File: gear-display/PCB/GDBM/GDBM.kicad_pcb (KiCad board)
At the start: 2 copper layers, 96 x 87 mm, 91 parts, among them J1 Con_Screw_1x04_691313510004, J2 Con_Screw_1x04_691313510004, J3 DC_2.5_5.5_PJ-090BH, J4 Con_Screw_1x04_691313510004, J5 Con_Screw_1x04_691313510004, J6 Con_Screw_1x04_691313510004, J7 Con_Screw_1x04_691313510004, J8 USB_B_V_Adam_USB-B-S-VT, M1 Knob_6mm_BL_RED_CLIFF_CL17084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, Q1 PMOS_30V_4A1_SIL3407-TP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

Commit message: fixes
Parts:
- D3: footprint KD_Diode:LED_0603_1608Metric_Pad1.05x0.95mm_HandSolder -> KD_Diode:DIOC1608X70
- turned U1 to -90 degrees
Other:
- board text added: "Changes"
- board text added: "U4, D3, U1, 7-seg display footprints"

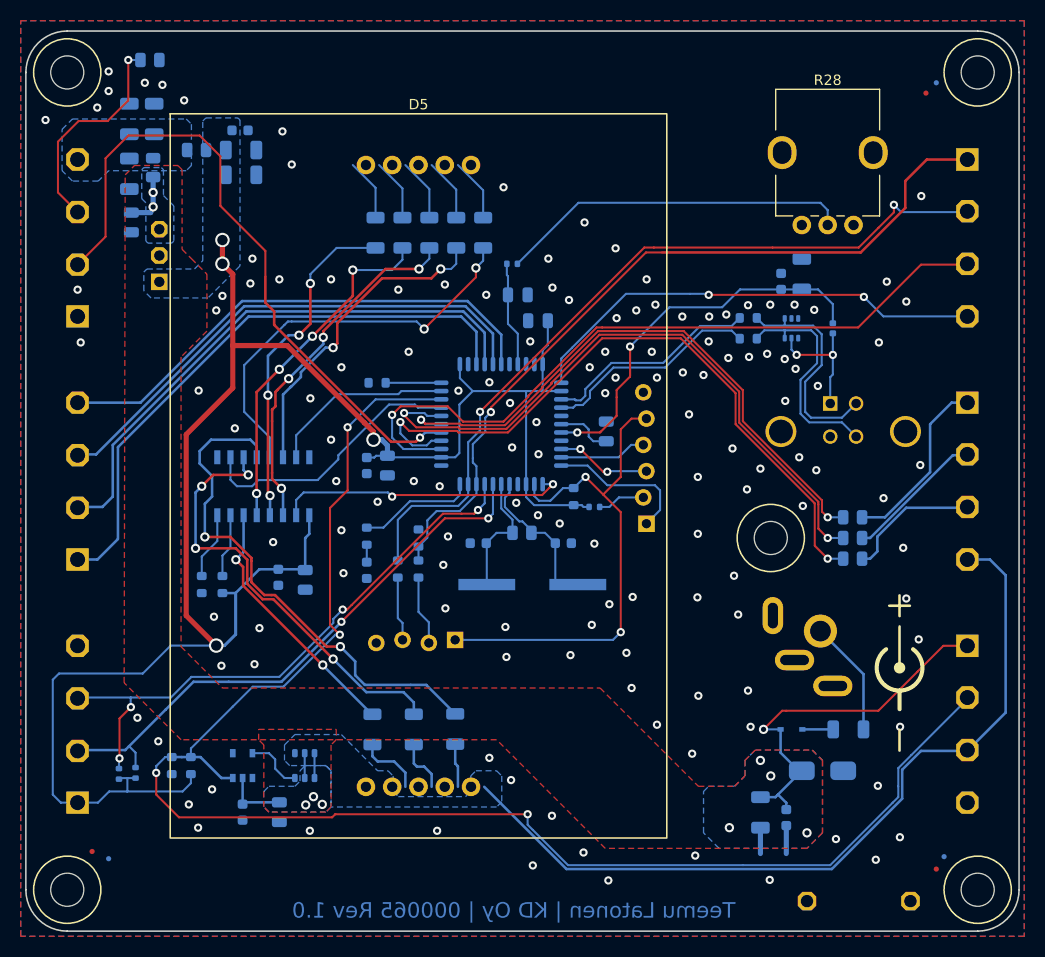
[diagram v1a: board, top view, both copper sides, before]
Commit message: bugfixes
added 555 circuit for brightness control
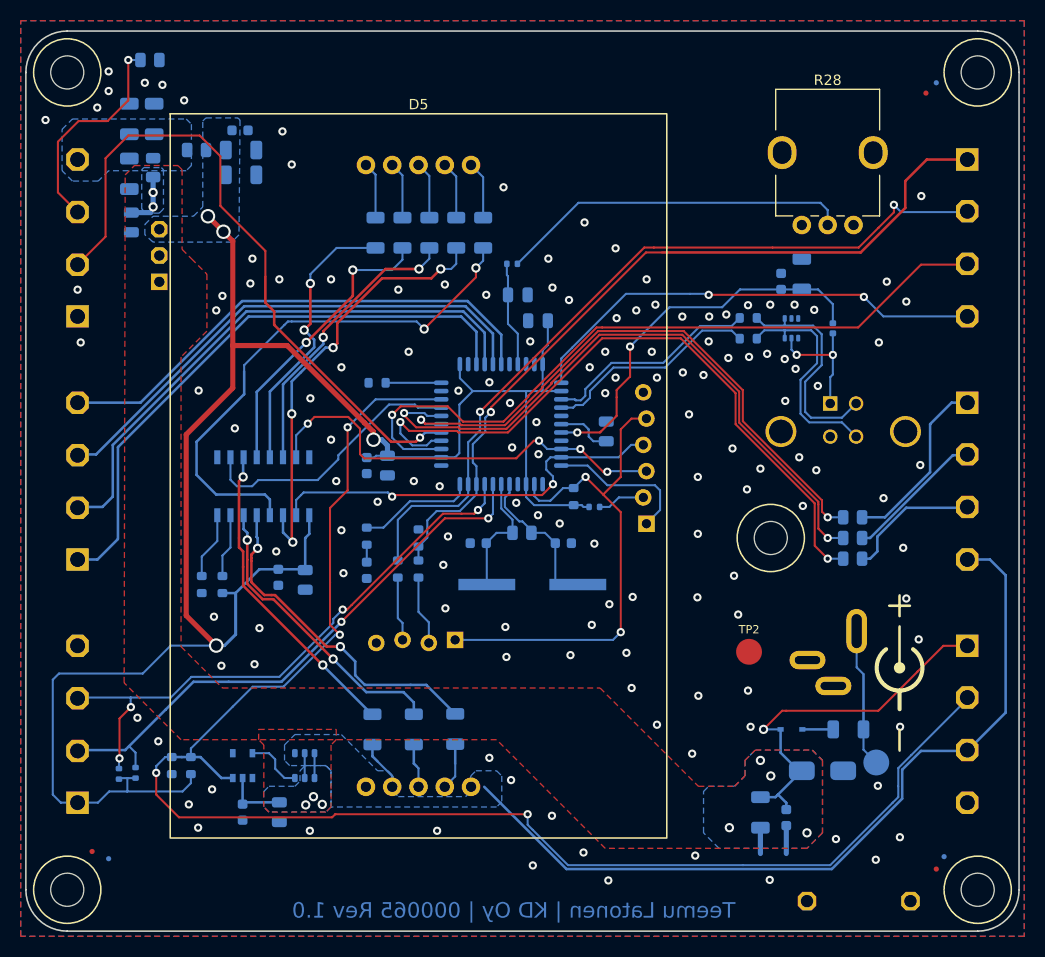
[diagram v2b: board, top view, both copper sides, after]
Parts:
- added TP1: TestPoint_2.5mm_Round, KD_Connector_Pads:TestPoint_Pad_D2.5mm, B.Cu at (165.2, 140.7)
- added TP2: TestPoint_2.5mm_Round, KD_Connector_Pads:TestPoint_Pad_D2.5mm, F.Cu at (152.9, 130.0)
- J3: value DC_2.5_5.5_PJ-090BH -> DC_2.1_5.5_54-00286; footprint KD_Connector_Circular:CON_DC_2.5_5.5_PJ-090BH -> KD_Connector_Circular:CON_DC_2.1_5.5_Tensility_54-00286
- U1: value DC_DC_5V_0A5_K78U05-500R3 -> DC_DC_5V_2A0_GAPTEC_OKI-78SR-5_H
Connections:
- net /MCU/A4(D22) renamed /Brightness Control/PWM_drive
- U2 pad 12: /LED Driver 3/SER_IN -> /MCU/D11
- U2 pad 32: /LED Driver 3/SRCK -> /MCU/D13
- U4 pad 11: /7-Segment Display/d -> /7-Segment Display/e
- U4 pad 12: /7-Segment Display/c -> /7-Segment Display/f
- U4 pad 13: /7-Segment Display/b -> /7-Segment Display/g
- U4 pad 14: /7-Segment Display/a -> /7-Segment Display/dp
- U4 pad 15: /LED Driver 3/SRCK -> /MCU/SCLK
- U4 pad 2: /LED Driver 3/SER_IN -> /MCU/MOSI
- U4 pad 3: /7-Segment Display/dp -> /7-Segment Display/a
- U4 pad 4: /7-Segment Display/g -> /7-Segment Display/b
- U4 pad 5: /7-Segment Display/f -> /7-Segment Display/c
- U4 pad 6: /7-Segment Display/e -> /7-Segment Display/d
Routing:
- net /MCU/SCLK: track 9.17 -> 41.9 mm, vias 2 -> 4
- net /MCU/MOSI: track 8.43 -> 39.7 mm, vias 0 -> 2
- net /LED Driver 3/SER_IN: track 28.2 -> 0.00 mm, vias 2 -> 0
- net /LED Driver 3/SRCK: track 18.0 -> 0.00 mm
- net /7-Segment Display/c: track 49.9 -> 32.5 mm
- net /7-Segment Display/d: track 42.8 -> 28.8 mm, vias 4 -> 2
- net /7-Segment Display/b: track 39.7 -> 51.7 mm
- net /7-Segment Display/a: track 31.1 -> 41.9 mm, vias 2 -> 4
- net /7-Segment Display/dp: track 34.4 -> 28.0 mm, vias 4 -> 2
- net /7-Segment Display/f: track 33.8 -> 28.3 mm, vias 4 -> 2
- net /7-Segment Display/g: track 32.9 -> 27.5 mm, vias 4 -> 2
- net /7-Segment Display/e: track 25.2 -> 30.4 mm
- net +5V: track 181.6 -> 184.5 mm
- net Net-(F1-Pad1): track 11.2 -> 13.5 mm
- net Net-(D5-Pad2): track 6.34 -> 4.88 mm
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
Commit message: layout
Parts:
- added C23: C_0603_10n_X7R_100V, KD_Capacitor:CAPC1608X90N, B.Cu at (141.0, 76.5)
- added C24: C_0603_10n_X7R_100V, KD_Capacitor:CAPC1608X90N, B.Cu at (132.5, 82.5)
- added D6: Schottky_30V_1A_Toshiba_CUS10S30, KD_Diode:D_SOD-323, B.Cu at (148.5, 81.0)
- added D7: Schottky_30V_1A_Toshiba_CUS10S30, KD_Diode:D_SOD-323, B.Cu at (146.0, 81.0)
- added R33: R_0805_1200_5%, KD_Resistor:RESC2012X60N, B.Cu at (147.0, 84.5)
- added U5: Timer_Oscillator_TLC555CDG4, KD_Package_SO:SOIC127P600X175-8, B.Cu at (139.0, 81.0)
- C1, C12, C16, C17, C18, C2, C3: value C_1206_10u_50V -> C_1206_10u_X5R_50V_automotive
- R29: value R_0402_4700_1% -> R_0603_DNP; footprint KD_Resistor:RESC1005X40N -> KD_Resistor:RESC1608X55N_DNP
- moved C21 13.8 mm to (141.6, 87.2)
- moved R29 9.36 mm to (136.1, 85.4), turned to 0 degrees
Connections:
- C21 pad 1: /Brightness Control/POT_W -> +5V
- R28 pad 1: +3V3 -> Net-(D7-Pad1)
- R28 pad 2: Net-(R28-Pad2) -> Net-(C24-Pad2)
- R28 pad 3: Earth -> Net-(D6-Pad2)
- R29 pad 1: Net-(R28-Pad2) -> /Brightness Control/PWM_drive
- R29 pad 2: /Brightness Control/POT_W -> Net-(C24-Pad2)
- U2 pad 31: /7-Segment Display/PWM -> /Brightness Control/PWM_drive
- U2 pad 40: /Brightness Control/PWM_drive -> /MCU/A4(D22)
- U2 pad 41: /Brightness Control/POT_W -> /7-Segment Display/PWM
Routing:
- net Net-(C24-Pad2): track 0.00 -> 51.5 mm
- net /7-Segment Display/PWM: track 152.9 -> 192.3 mm, vias 4 -> 7
- net +5V: track 184.5 -> 220.7 mm, vias 4 -> 6
- net Net-(R28-Pad2): track 34.2 -> 0.00 mm
- net Net-(D7-Pad1): track 0.00 -> 27.9 mm
- net /Brightness Control/PWM_drive: track 0.00 -> 27.5 mm, vias 0 -> 2
- net Net-(D6-Pad2): track 0.00 -> 13.9 mm
- net Net-(D6-Pad1): track 0.00 -> 12.8 mm
- net /Brightness Control/POT_W: track 10.1 -> 0.00 mm
- net Net-(C23-Pad1): track 0.00 -> 2.63 mm
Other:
- board text added: "Teemu Latonen | KD Oy | 000065 Rev 2.0"
- board text removed: "Teemu Latonen | KD Oy | 000065 Rev 1.0"

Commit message: Added a ferrite and silk screen markings
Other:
- board text added: "+"
- board text added: "-"
- board text added: "B"
- board text added: "D"
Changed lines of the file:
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@@
     (effects (font (size 1.5 1.5) (thickness 0.3)) (justify mirror))
+  )
+  (gr_text "+" (at 85.1 82.4) (layer "F.SilkS")
+    (effects (font (size 1.5 1.5) (thickness 0.2)))
+  )
+  (gr_text "D" (at 85.1 92.6) (layer "F.SilkS")
+    (effects (font (size 1.5 1.5) (thickness 0.2)))
+  )
+  (gr_text "-" (at 85.1 97.5) (layer "F.SilkS")
+    (effects (font (size 1.5 1.5) (thickness 0.2)))
+  )
+  (gr_text "B" (at 85.1 87.6) (layer "F.SilkS")
+    (effects (font (size 1.5 1.5) (thickness 0.2)))
   )
   (gr_text "Changes" (at 102 193.5) (layer "Cmts.User")

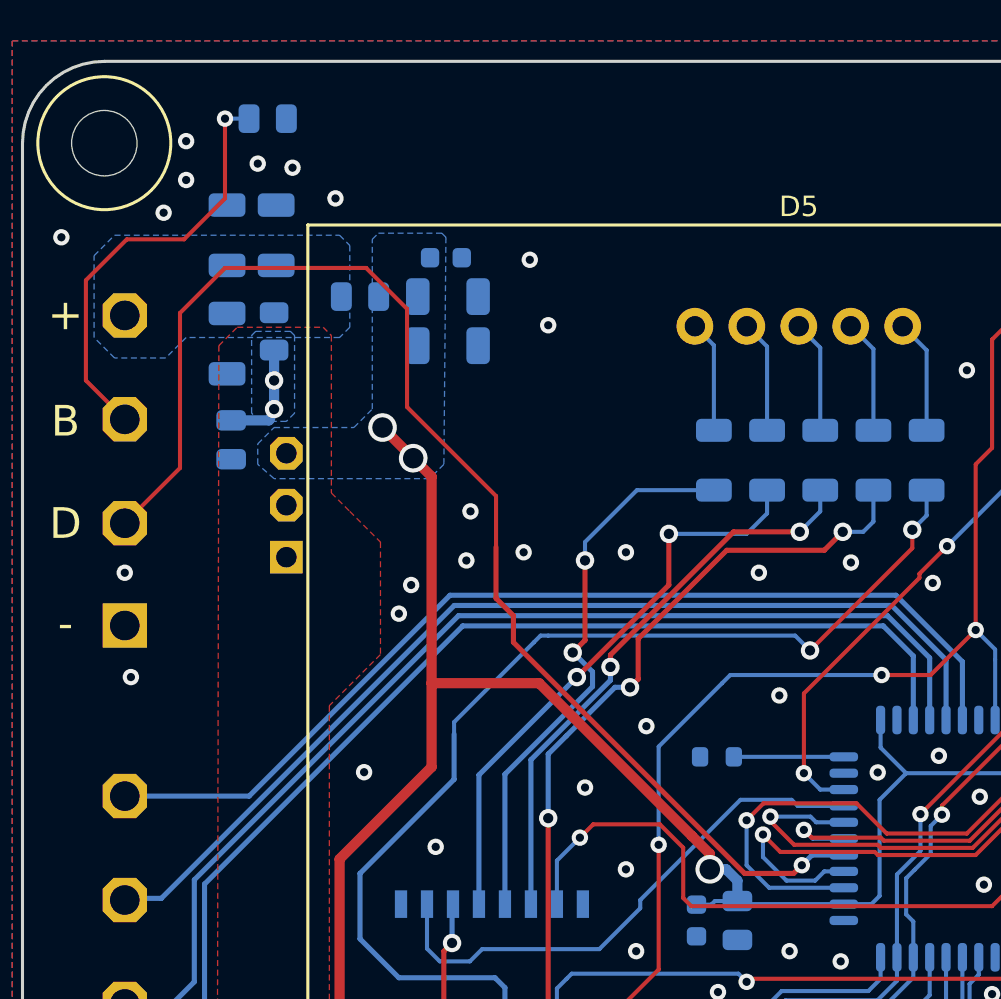
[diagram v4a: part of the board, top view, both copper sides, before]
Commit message: led buffer added
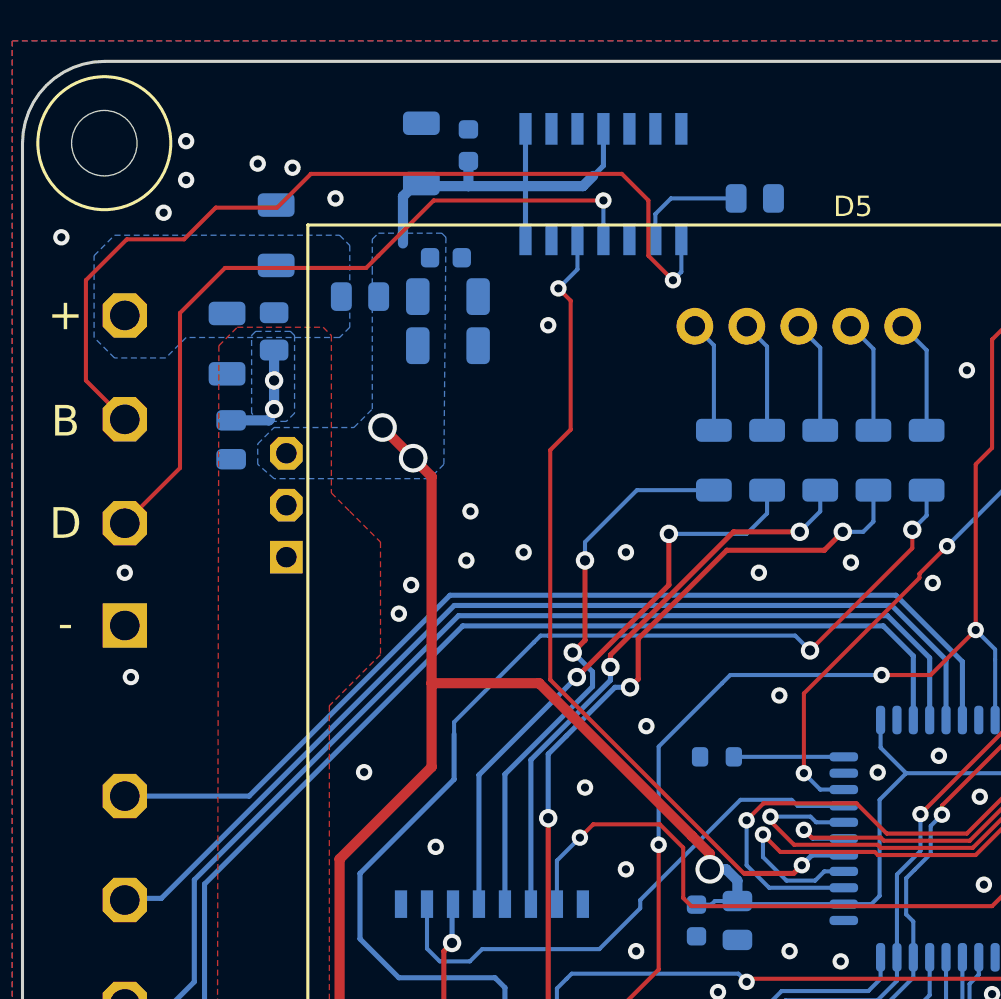
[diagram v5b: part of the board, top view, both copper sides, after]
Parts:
- added C25: C_1206_10u_X5R_50V_automotive, KD_Capacitor:CAPC3216X150N, B.Cu at (102.5, 74.5)
- added U8: Buffer_74LVC125AS14-13_DIODES, KD_Package_SO:SOIC127P600X175-14N, B.Cu at (111.4, 76.0)
- C18: value C_1206_10u_X5R_50V_automotive -> C_0603_100n_X7R_100V; footprint KD_Capacitor:CAPC3216X150N -> KD_Capacitor:CAPC1608X90N
- moved R21 24.1 mm to (118.8, 76.7)
- moved C18 12.6 mm to (104.8, 74.1)
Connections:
- C18 pad 1: /RPM Bar/LED_PWR -> +5V
- J4 pad 2: /MCU/D6 -> Net-(J4-Pad2)
- J4 pad 3: /RPM Bar/LED_STRIP_B -> Net-(J4-Pad3)
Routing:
- net Net-(J4-Pad3): track 0.00 -> 44.3 mm, vias 0 -> 1
- net Net-(J4-Pad2): track 0.00 -> 36.3 mm, vias 0 -> 1
- net /MCU/D6: track 63.9 -> 41.2 mm, vias 1 -> 2
- net +5V: track 220.7 -> 241.9 mm
- net /RPM Bar/LED_STRIP_B: track 21.1 -> 5.50 mm, vias 1 -> 0
- net Earth: vias 138 -> 137

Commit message: documentation
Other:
- board text added: "U4, D3, U1, 7-seg display footprints. U8 added."
- board text removed: "U4, D3, U1, 7-seg display footprints"
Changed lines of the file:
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@@
     (effects (font (size 1.5 1.5) (thickness 0.3)) (justify mirror))
+  )
+  (gr_text "-" (at 85.1 97.5) (layer "F.SilkS")
+    (effects (font (size 1.5 1.5) (thickness 0.2)))
   )
   (gr_text "+" (at 85.1 82.4) (layer "F.SilkS")
@@
   )
   (gr_text "D" (at 85.1 92.6) (layer "F.SilkS")
-    (effects (font (size 1.5 1.5) (thickness 0.2)))
-  )
-  (gr_text "-" (at 85.1 97.5) (layer "F.SilkS")
     (effects (font (size 1.5 1.5) (thickness 0.2)))
   )
@@
     (effects (font (size 2 2) (thickness 0.3)) (justify left))
   )
-  (gr_text "U4, D3, U1, 7-seg display footprints" (at 102 196.5) (layer "Cmts.User")
+  (gr_text "U4, D3, U1, 7-seg display footprints. U8 added." (at 102 196.5) (layer "Cmts.User")
     (effects (font (size 1 1) (thickness 0.25)) (justify left))
   )

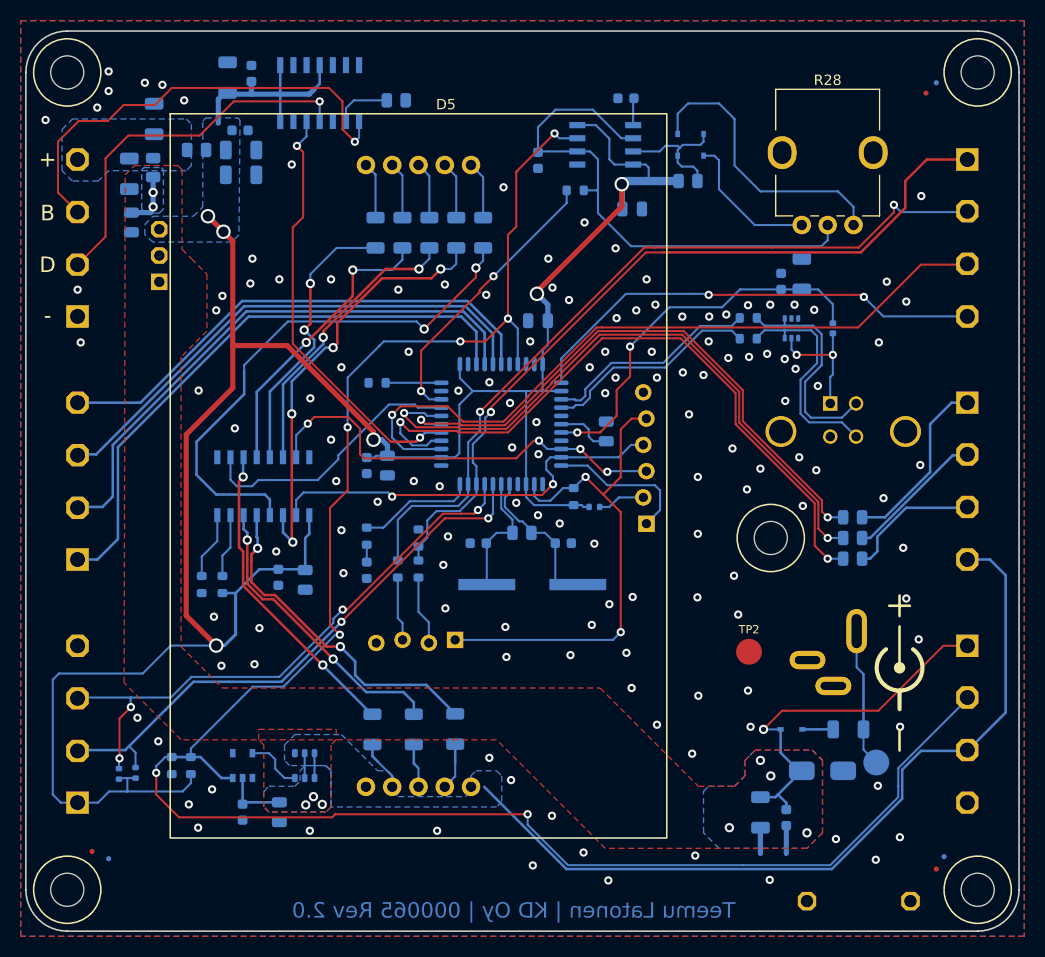
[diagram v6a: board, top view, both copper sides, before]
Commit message: change to kicad 7
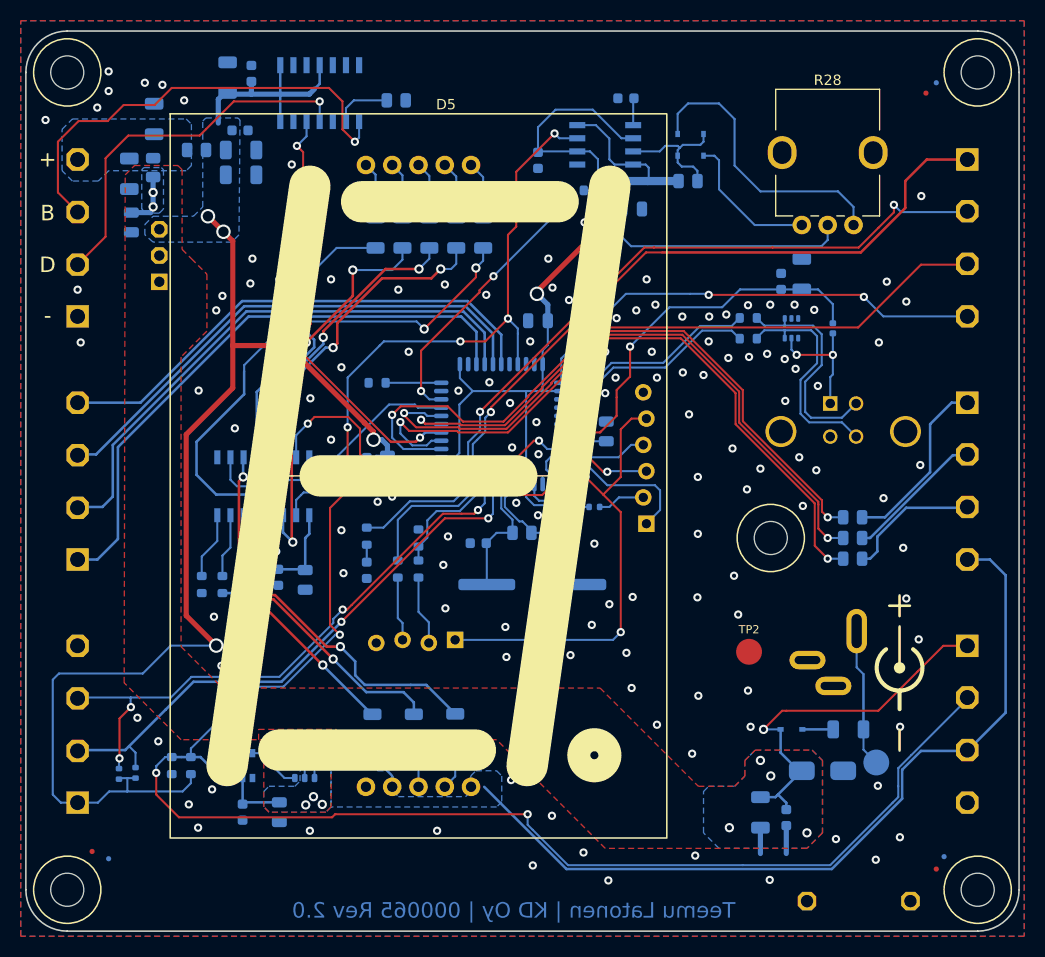
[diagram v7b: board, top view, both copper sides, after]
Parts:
- D3: footprint KD_Diode:DIOC1608X70 -> KD_Diode:DIOC1608X70N
- turned X3 to 180 degrees
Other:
- board text added: "1:V+ 2:D 3:B 4:GND"
